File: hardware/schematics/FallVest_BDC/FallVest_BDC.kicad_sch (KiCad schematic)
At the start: 10 parts, among them IC1 ATGM336H-5N31, J1 Actuator, J2 MG90S_SERVO, Q1 AO3400A, U1 SIM800L-CORE, U2 ESP32-WROOM-32, U3 MPU-6050

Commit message: Replaced bare module
- Development board ELEGOO
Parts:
- removed U2: ESP32-WROOM-32, RF_Module:ESP32-WROOM-32, symbol RF_Module:ESP32-WROOM-32
- added ELEGOO_ESP32: Development Board, symbol Connector_Generic:Conn_02x15_Odd_Even
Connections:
- net +3V3: now also ELEGOO_ESP32.30 (Pin_30)
- net GND: now also ELEGOO_ESP32.28 (Pin_28)
- net at Q1.3 (D), R.2: now also ELEGOO_ESP32.2 (Pin_2)
- net at IC1.2 (TXD): now also ELEGOO_ESP32.18 (Pin_18)
- net at IC1.3 (RXD): now also ELEGOO_ESP32.20 (Pin_20)
- net at U3.12 (INT): now also ELEGOO_ESP32.9 (Pin_9)
- net at U3.23 (SCL): now also ELEGOO_ESP32.10 (Pin_10)
- net at U3.24 (SDA): now also ELEGOO_ESP32.4 (Pin_4)
- net at R1.2: now also ELEGOO_ESP32.15 (Pin_15)

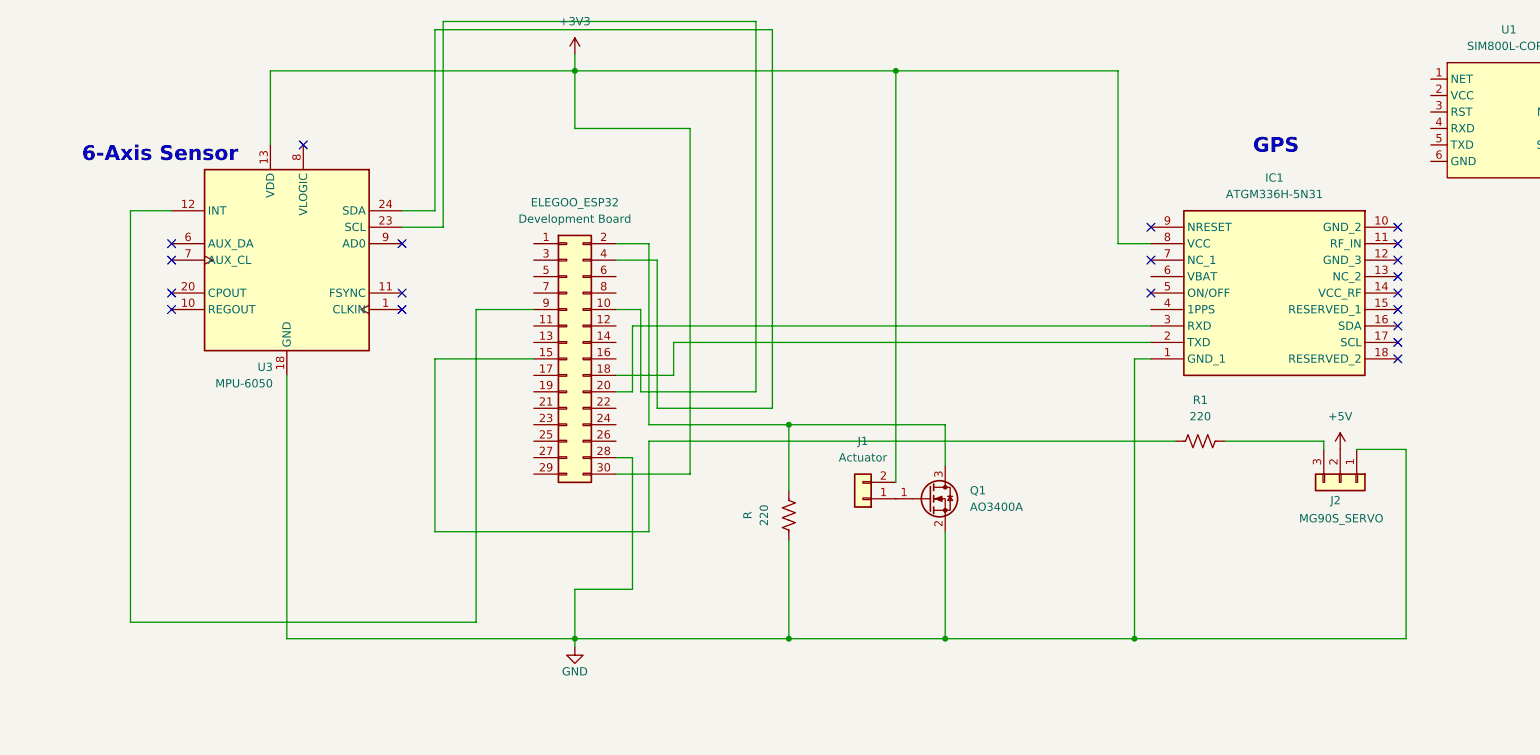
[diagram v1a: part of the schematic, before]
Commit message: Fix scheamtic
Nets need to be put on ESP32 and wiring is messed up (double check)
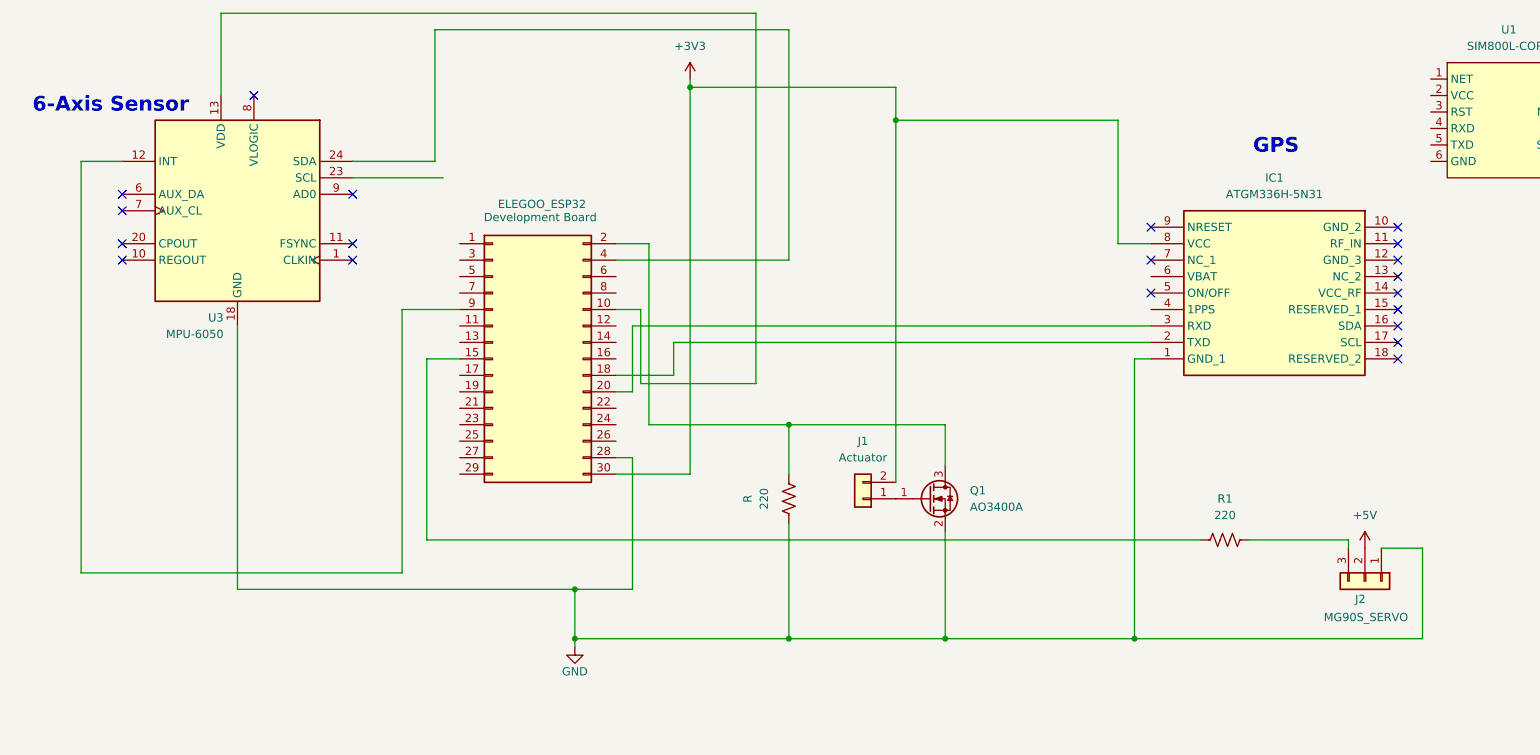
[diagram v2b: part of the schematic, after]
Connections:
- net +3V3: no longer U3.13 (VDD)
- net at ELEGOO_ESP32.10 (Pin_10): now also U3.13 (VDD); no longer U3.23 (SCL)
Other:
- moved on the sheet: ELEGOO_ESP32, J2, R, R1, U3

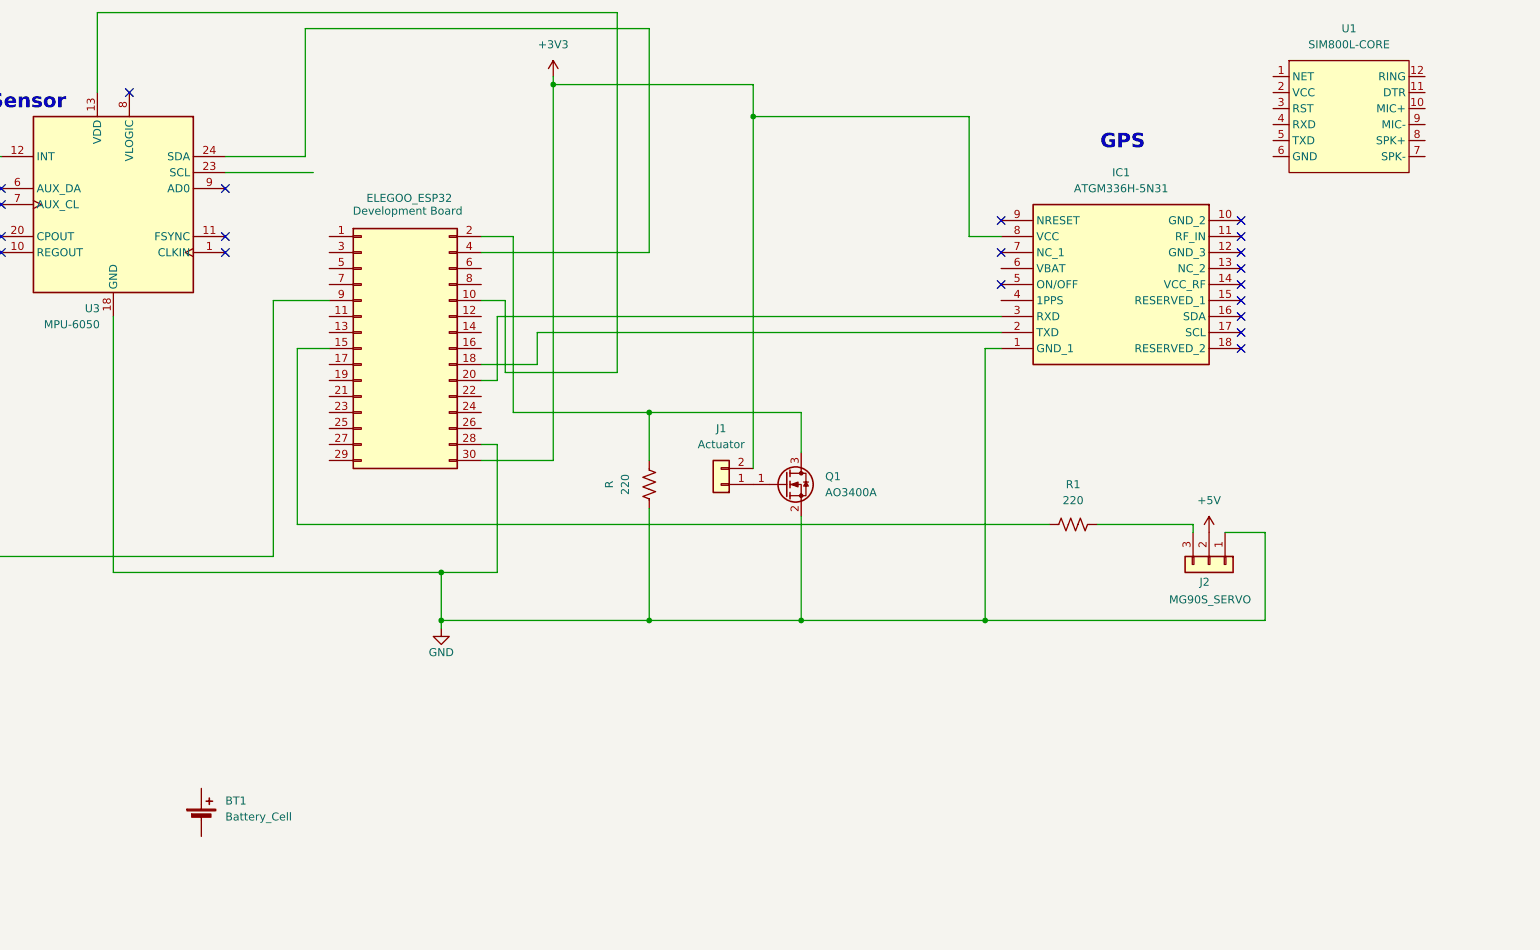
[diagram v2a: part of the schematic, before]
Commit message: Added Converter
Schematic needs to still be fixed up
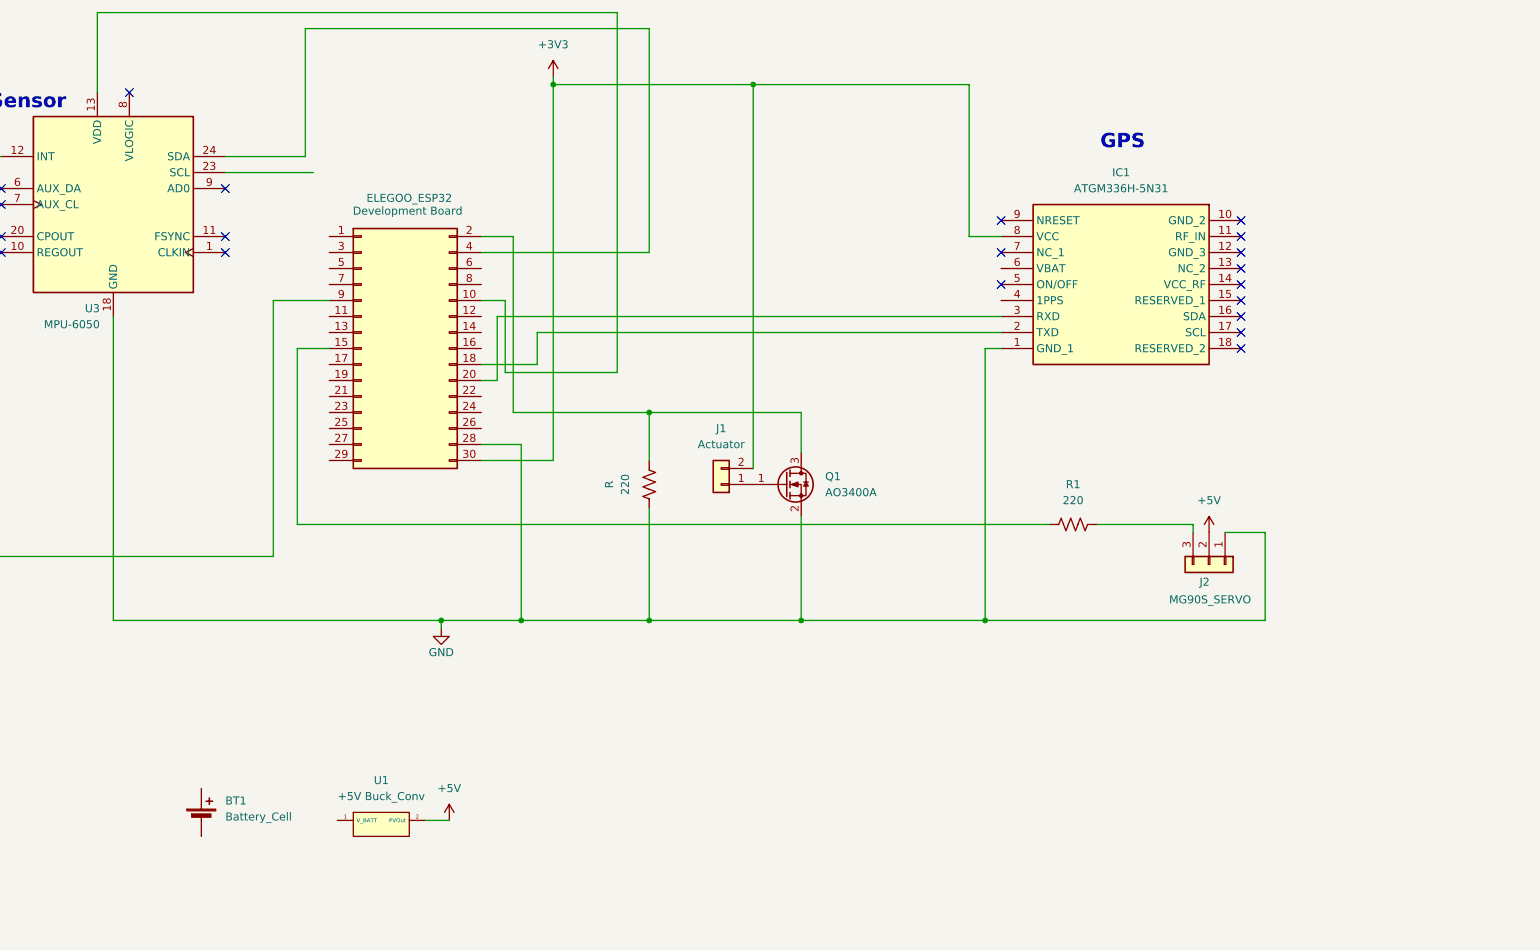
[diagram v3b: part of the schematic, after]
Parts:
- removed U1: SIM800L-CORE, symbol sim800l-core:SIM800L-CORE
- added U1: +5V Buck_Conv, symbol Custom:Buck_Conv_(+5V)
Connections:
- net +5V: now also U1.2 (PVOut)
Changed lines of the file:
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@@
 	)
 	(junction
-		(at 116.84 27.94)
+		(at 148.59 27.94)
 		(diameter 0)
 		(color 0 0 0 0)
 	)
 	(junction
-		(at 99.06 105.41)
+		(at 111.76 113.03)
 		(diameter 0)
 		(color 0 0 0 0)
 	)
 	(junction
-		(at 99.06 113.03)
+		(at 116.84 27.94)
 		(diameter 0)
 		(color 0 0 0 0)
 	)
 	(junction
-		(at 132.08 113.03)
+		(at 99.06 113.03)
 		(diameter 0)
 		(color 0 0 0 0)
 	)
 	(junction
-		(at 148.59 33.02)
+		(at 132.08 113.03)
 		(diameter 0)
 		(color 0 0 0 0)
@@
 	(wire
 		(pts
+			(xy 96.52 144.78) (xy 100.33 144.78)
+		)
+		(stroke
+			(width 0)
+			(type default)
+		)
+	)
+	(wire
+		(pts
 			(xy 182.88 52.07) (xy 187.96 52.07)
 		)
@@
 	(wire
 		(pts
-			(xy 46.99 64.77) (xy 46.99 105.41)
+			(xy 46.99 64.77) (xy 46.99 113.03)
 		)
 		(stroke
@@
 	(wire
 		(pts
-			(xy 99.06 105.41) (xy 99.06 113.03)
-		)
-		(stroke
-			(width 0)
-			(type default)
-		)
-	)
-	(wire
-		(pts
-			(xy 182.88 33.02) (xy 182.88 52.07)
+			(xy 182.88 27.94) (xy 182.88 52.07)
 		)
 		(stroke
@@
 	(wire
 		(pts
-			(xy 107.95 105.41) (xy 99.06 105.41)
+			(xy 46.99 113.03) (xy 99.06 113.03)
 		)
 		(stroke
@@
 	(wire
 		(pts
-			(xy 46.99 105.41) (xy 99.06 105.41)
+			(xy 105.41 72.39) (xy 114.3 72.39)
 		)
 		(stroke
@@
 	(wire
 		(pts
-			(xy 105.41 72.39) (xy 114.3 72.39)
+			(xy 148.59 27.94) (xy 148.59 88.9)
 		)
 		(stroke
@@
 	(wire
 		(pts
-			(xy 148.59 27.94) (xy 148.59 33.02)
+			(xy 132.08 113.03) (xy 156.21 113.03)
 		)
 		(stroke
@@
 	(wire
 		(pts
-			(xy 132.08 113.03) (xy 156.21 113.03)
+			(xy 111.76 85.09) (xy 111.76 113.03)
 		)
 		(stroke
@@
 	(wire
 		(pts
-			(xy 107.95 85.09) (xy 107.95 105.41)
+			(xy 64.77 39.37) (xy 77.47 39.37)
 		)
 		(stroke
@@
 	(wire
 		(pts
-			(xy 64.77 39.37) (xy 77.47 39.37)
+			(xy 111.76 113.03) (xy 132.08 113.03)
 		)
 		(stroke
@@
 	(wire
 		(pts
-			(xy 148.59 33.02) (xy 182.88 33.02)
+			(xy 148.59 27.94) (xy 182.88 27.94)
 		)
 		(stroke
@@
 	(wire
 		(pts
-			(xy 99.06 113.03) (xy 132.08 113.03)
+			(xy 99.06 113.03) (xy 111.76 113.03)
 		)
 		(stroke
@@
 	(wire
 		(pts
-			(xy 105.41 85.09) (xy 107.95 85.09)
+			(xy 105.41 85.09) (xy 111.76 85.09)
 		)
 		(stroke
@@
 		)
 	)
-	(wire
-		(pts
-			(xy 148.59 33.02) (xy 148.59 88.9)
-		)
-		(stroke
-			(width 0)
-			(type default)
-		)
-	)
 	(image
 		(at -96.52 171.45)
@@
 	)
 	(image
-		(at -58.42 113.03)
+		(at -43.18 114.3)
+		(scale 1.78501)
 		(data "iVBORw0KGgoAAAANSUhEUgAAAj0AAAEsCAYAAAAo8wKiAAAABHNCSVQICAgIfAhkiAAAIABJREFU"
 			"eJzsvVmQZcl53/fLzLPfrW4tXUvvs2+YwcxgAG6AQZEiGaLCdJCmQFnhkEWFKDpsR1iOkJ8Z1oMe"
@@
 	)
 	(image
-		(at -58.42 73.66)
+		(at -40.64 60.96)
+		(scale 1.45915)
 		(data "iVBORw0KGgoAAAANSUhEUgAAAqQAAAHTCAYAAADxiQpNAAAABHNCSVQICAgIfAhkiAAAIABJREFU"
 			"eJzsnXd8XNWZsJ9z750mTVGxLcu23LCNAVds44bBlAAGTHUSAqH9NpDCpvw2ENj9NuskBBY2hmRh"
@@
 	)
 	(symbol
+		(lib_id "power:+3V3")
+		(at 100.33 144.78 0)
+		(unit 1)
+		(exclude_from_sim no)
+		(in_bom yes)
+		(on_board yes)
+		(dnp no)
+		(fields_autoplaced yes)
+		(property "Reference" "#PWR03"
+			(at 100.33 148.59 0)
+			(effects
+				(font
+					(size 1.27 1.27)
+				)
+				(hide yes)
+			)
+		)
+		(property "Value" "+5V"
+			(at 100.33 139.7 0)
+			(effects
+				(font
+					(size 1.27 1.27)
+				)
+			)
+		)
+		(property "Footprint" ""
+			(at 100.33 144.78 0)
+			(effects
+				(font
+					(size 1.27 1.27)
+				)
+				(hide yes)
+			)
+		)
+		(property "Datasheet" ""
+			(at 100.33 144.78 0)
+			(effects
+				(font
+					(size 1.27 1.27)
+				)
+				(hide yes)
+			)
+		)
+		(property "Description" "Power symbol creates a global label with name \"+3V3\""
+			(at 100.33 144.78 0)
+			(effects
+				(font
+					(size 1.27 1.27)
+				)
+				(hide yes)
+			)
+		)
+		(pin "1"
+		)
+		(instances
+			(project "FallVest_BDC"
+				(path "/74063a4b-f2d6-40f5-8694-30dc3de3f53f"
+					(reference "#PWR03")
+					(unit 1)
+				)
+			)
+		)
+	)
+	(symbol
 		(lib_id "sim800l-core:ATGM336H-5N31")
 		(at 226.06 49.53 0)
@@
 	)
 	(symbol
+		(lib_id "Custom:Buck_Conv_(+5V)")
+		(at 83.82 140.97 0)
+		(unit 1)
+		(exclude_from_sim no)
+		(in_bom yes)
+		(on_board yes)
+		(dnp no)
+		(fields_autoplaced yes)
+		(property "Reference" "U1"
+			(at 89.535 138.43 0)
+			(effects
+				(font
+					(size 1.27 1.27)
+				)
+			)
+		)
+		(property "Value" "+5V Buck_Conv"
+			(at 89.535 140.97 0)
+			(effects
+				(font
+					(size 1.27 1.27)
+				)
+			)
+		)
+		(property "Footprint" ""
+			(at 83.82 140.97 0)
+			(effects
+				(font
+					(size 1.27 1.27)
+				)
+				(hide yes)
+			)
+		)
+		(property "Datasheet" ""
+			(at 83.82 140.97 0)
+			(effects
+				(font
+					(size 1.27 1.27)
+				)
+				(hide yes)
+			)
+		)
+		(property "Description" ""
+			(at 83.82 140.97 0)
+			(effects
+				(font
+					(size 1.27 1.27)
+				)
+				(hide yes)
+			)
+		)
+		(pin "1"
+		)
+		(pin "2"
+		)
+		(instances
+			(project ""
+				(path "/74063a4b-f2d6-40f5-8694-30dc3de3f53f"
+					(reference "U1")
+					(unit 1)
+				)
+			)
+		)
+	)
+	(symbol
 		(lib_id "power:+3V3")
 		(at 220.98 99.06 0)
@@
 					(unit 1)
 				)
-			)
-		)
-	)
-	(symbol
-		(lib_id "sim800l-core:SIM800L-CORE")
-		(at 242.57 31.75 0)
-		(unit 1)
-		(exclude_from_sim no)
-		(in_bom yes)
-		(on_board yes)
-		(dnp no)
-		(fields_autoplaced yes)
-		(property "Reference" "U1"
-			(at 243.205 19.05 0)
-			(effects
-				(font
-					(size 1.27 1.27)
-				)
-			)
-		)
-		(property "Value" "SIM800L-CORE"
-			(at 243.205 21.59 0)
-			(effects
-				(font
-					(size 1.27 1.27)
-				)
-			)
-		)
-		(property "Footprint" ""
-			(at 242.57 31.75 0)
-			(effects
-				(font
-					(size 1.27 1.27)
-				)
-				(hide yes)
-			)
-		)
-		(property "Datasheet" ""
-			(at 242.57 31.75 0)
-			(effects
-				(font
-					(size 1.27 1.27)
-				)
-				(hide yes)
-			)
-		)
-		(property "Description" ""
-			(at 242.57 31.75 0)
-			(effects
-				(font
-					(size 1.27 1.27)
-				)
-				(hide yes)
-			)
-		)
-		(pin "4"
-		)
-		(pin "10"
-		)
-		(pin "3"
-		)
-		(pin "9"
-		)
-		(pin "12"
-		)
-		(pin "1"
-		)
-		(pin "8"
-		)
-		(pin "11"
-		)
-		(pin "2"
-		)
-		(pin "7"
-		)
-		(pin "6"
-		)
-		(pin "5"
-		)
-		(instances
-			(project ""
-				(path "/74063a4b-f2d6-40f5-8694-30dc3de3f53f"
-					(reference "U1")
-					(unit 1)
-				)
